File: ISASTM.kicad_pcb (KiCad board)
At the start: 4 copper layers, 101.6 x 101.6 mm, 137 parts, among them J1 Bus_ISA_8bit, J2 USB_C_Receptacle_USB2.0, J3 Boot select, J4 USB_C_Receptacle_USB2.0, J5 TagConnect_TC2030_SWD, SW1 Reset, U1 STM32H743IITx, U10 SN74AVC8T245PW, U11 SN74AVC8T245PW, U12 SN74AVC8T245PW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

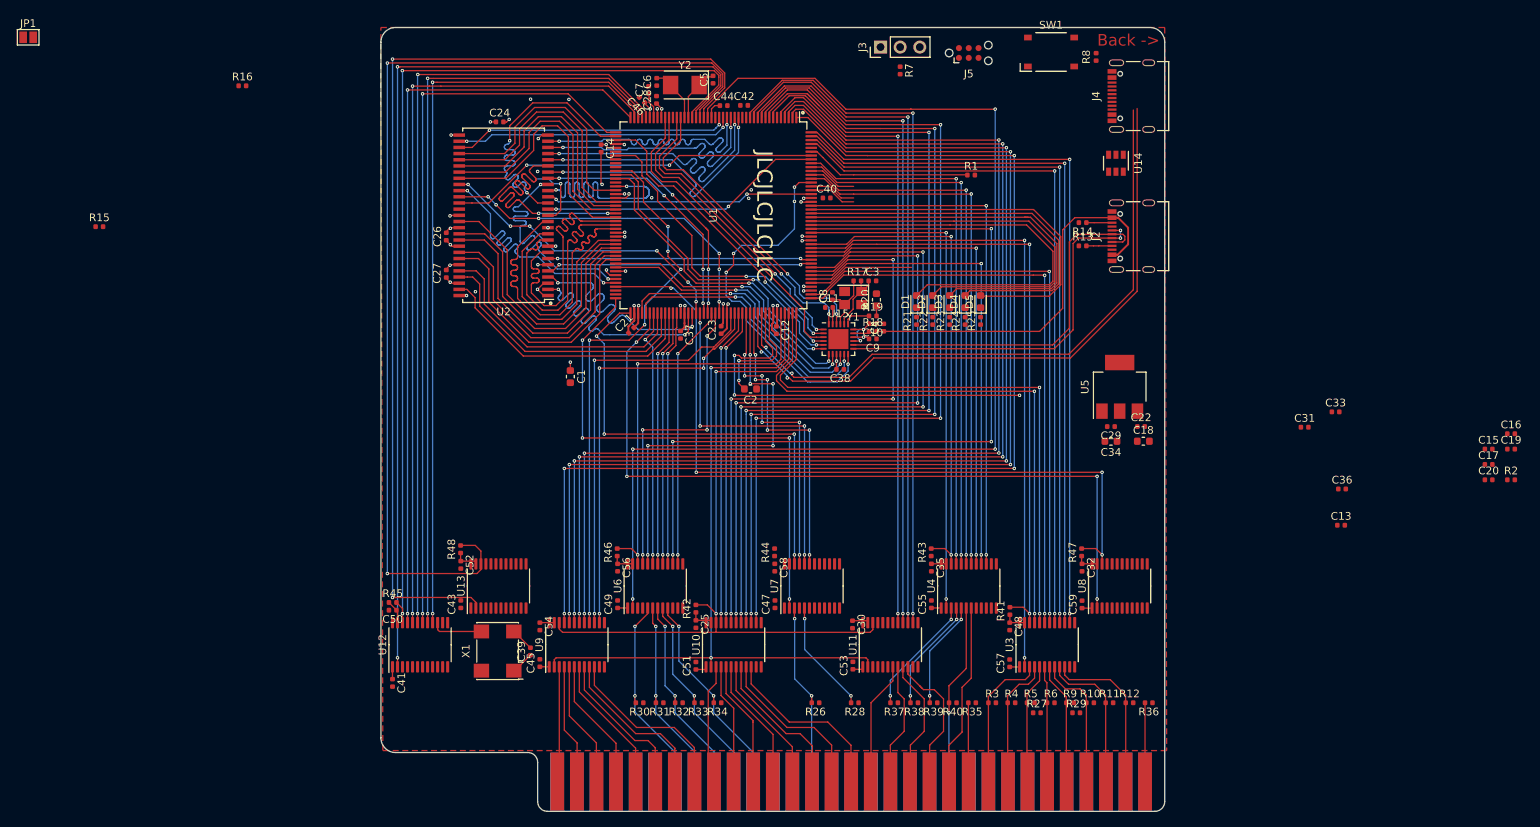
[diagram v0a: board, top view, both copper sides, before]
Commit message: Finish ISA signal routing
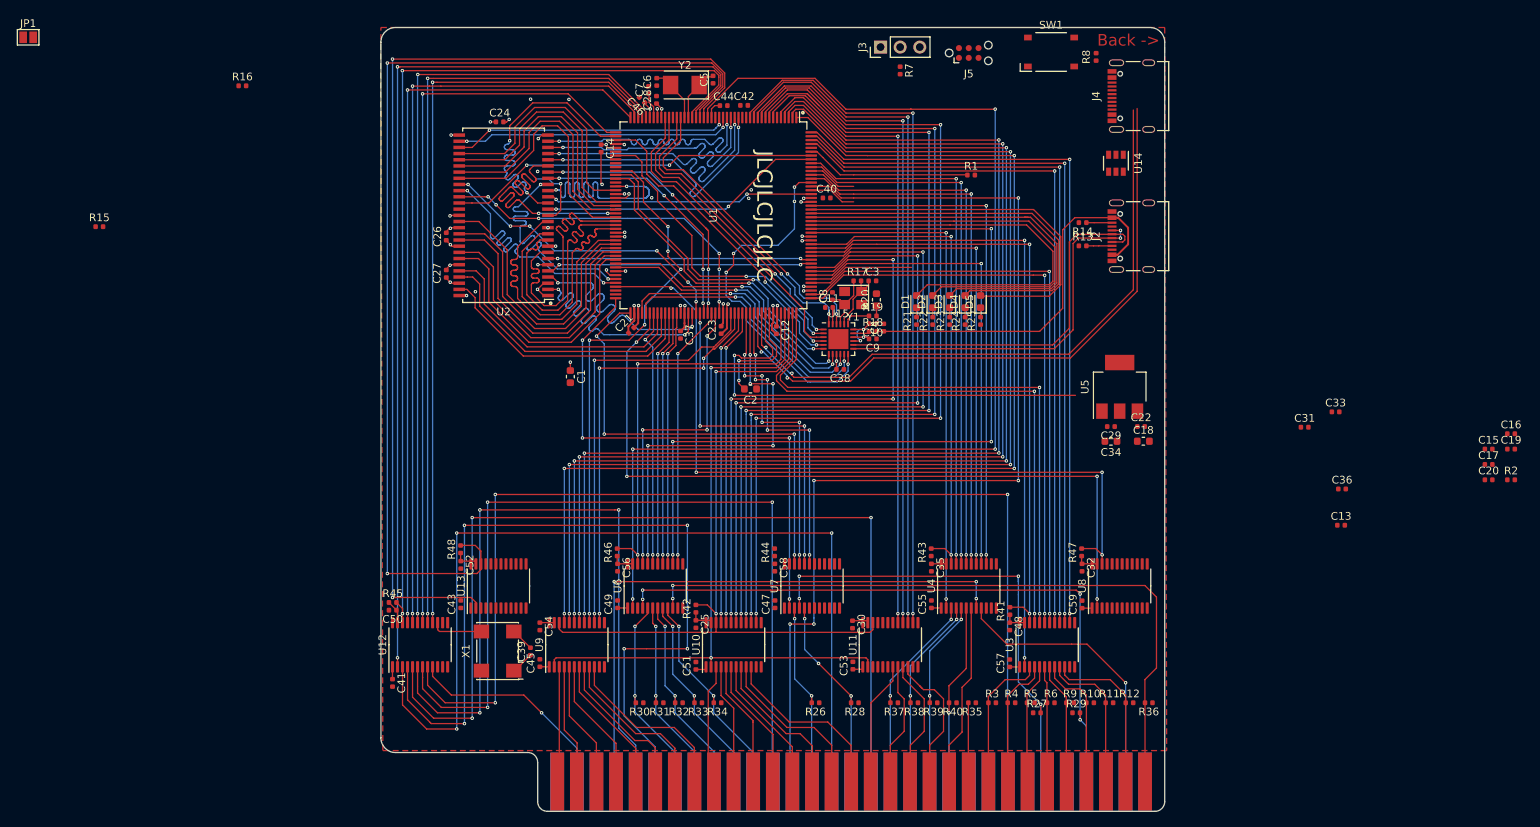
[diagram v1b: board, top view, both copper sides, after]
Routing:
- net /~NOWS: track 0.00 -> 142.8 mm, vias 0 -> 3
- net /~DACK3: track 0.00 -> 125.9 mm, vias 0 -> 3
- net /~REFRESH: track 6.12 -> 131.7 mm, vias 0 -> 5
- net /~DACK1: track 0.00 -> 119.8 mm, vias 0 -> 3
- net /CLK: track 0.00 -> 112.2 mm, vias 0 -> 3
- net /~DACK2: track 0.00 -> 110.7 mm, vias 0 -> 5
- net /TC: track 0.00 -> 93.1 mm, vias 0 -> 3
- net /IRQ2: track 0.00 -> 84.8 mm, vias 0 -> 4
- net /~IO_CH_CK: track 10.5 -> 91.1 mm, vias 0 -> 2
- net /ALE: track 0.00 -> 76.0 mm, vias 0 -> 3
- net /DRQ2: track 0.00 -> 59.7 mm, vias 0 -> 4
- net /ISARESET: track 0.00 -> 36.3 mm, vias 0 -> 1
- net /OSC: track 0.00 -> 28.2 mm, vias 0 -> 1
- net /~IOR: track 15.6 -> 27.3 mm
- net /~SMEMR: track 14.0 -> 25.4 mm
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
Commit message: Finish routing
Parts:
- C13, C17, C36: moved to B.Cu
- moved JP1 139.7 mm to (108.3, 31.8), turned to 270 degrees
- moved R15 129.1 mm to (106.9, 24.7)
- moved C17 124.5 mm to (37.9, 41.6), turned to 90 degrees
- moved R2 124.3 mm to (48.4, 22.2)
- moved R16 109.6 mm to (106.9, 21.7), turned to 180 degrees
- moved C13 109.5 mm to (34.4, 49.1), turned to 180 degrees
- moved C36 107.8 mm to (35.6, 47.0), turned to 90 degrees
- moved C31 100.0 mm to (39.1, 37.9), turned to 270 degrees
- moved C16 95.3 mm to (73.2, 31.9), turned to 315 degrees
- moved C19 92.9 mm to (73.0, 41.8)
- moved C20 90.2 mm to (71.3, 51.5), turned to 270 degrees
- moved C15 88.0 mm to (85.9, 20.0), turned to 180 degrees
- moved C33 62.7 mm to (97.2, 17.8), turned to 270 degrees
- moved C39 28.6 mm to (34.7, 66.9)
- moved X1 28.6 mm to (30.5, 66.8)
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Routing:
- net +5V: track 12.4 -> 151.8 mm, vias 1 -> 45
- net /SWDIO: track 60.5 -> 128.8 mm, vias 2 -> 6
- net /~RESET: track 40.2 -> 101.8 mm, vias 2 -> 5
- net +3V3: track 76.9 -> 135.5 mm, vias 21 -> 95
- net /IO_CH_RDY: track 10.3 -> 68.7 mm, vias 0 -> 2
- net /SWCLK: track 13.8 -> 70.3 mm, vias 0 -> 4
- net /SWO: track 6.12 -> 56.7 mm, vias 0 -> 4
- net /BOOT0: track 6.33 -> 51.5 mm, vias 0 -> 2
- net GND: track 37.1 -> 72.1 mm, vias 27 -> 116
- net Net-(J4-PadA4): track 0.00 -> 28.0 mm, vias 0 -> 6
- net Net-(U12-Pad15): track 6.65 -> 33.3 mm, vias 0 -> 2
- net /USB_FS_D+: track 82.4 -> 90.6 mm
- net /USB_FS_D-: track 84.2 -> 92.4 mm, vias 2 -> 4
- net /~CONTROL2_OE: track 60.2 -> 63.1 mm
- net Net-(J4-PadA5): track 0.00 -> 2.74 mm
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- added copper zone on F.Cu, net +3V3
- added copper zone on In2.Cu, net +5V
- added copper zone on B.Cu, net GND

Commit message: Stitch board edge
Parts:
- moved C43 0.14 mm to (25.6, 89.5)
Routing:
- net GND: vias 116 -> 389

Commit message: Finish GND stitching
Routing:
- net GND: vias 389 -> 470
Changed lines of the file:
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@@
     (thickness 1.6)
     (drawings 35)
-    (tracks 4887)
+    (tracks 4968)
     (zones 0)
     (modules 137)
@@
   (gr_arc (start 115.57 114.935) (end 115.57 116.205) (angle -90) (layer Edge.Cuts) (width 0.05))
   (gr_arc (start 36.83 114.935) (end 35.56 114.935) (angle -90) (layer Edge.Cuts) (width 0.05))
+  (via (at 55.9 79.6) (size 0.45) (drill 0.2) (layers F.Cu B.Cu) (net 32))
+  (via (at 55.9 80.6) (size 0.45) (drill 0.2) (layers F.Cu B.Cu) (net 32))
+  (via (at 55.9 75.6) (size 0.45) (drill 0.2) (layers F.Cu B.Cu) (net 32))
+  (via (at 55.9 78.6) (size 0.45) (drill 0.2) (layers F.Cu B.Cu) (net 32))
+  (via (at 55.9 74.6) (size 0.45) (drill 0.2) (layers F.Cu B.Cu) (net 32))
+  (via (at 55.9 77.6) (size 0.45) (drill 0.2) (layers F.Cu B.Cu) (net 32))
+  (via (at 55.9 76.6) (size 0.45) (drill 0.2) (layers F.Cu B.Cu) (net 32))
+  (via (at 47.4 79.6) (size 0.45) (drill 0.2) (layers F.Cu B.Cu) (net 32))
+  (via (at 47.4 80.6) (size 0.45) (drill 0.2) (layers F.Cu B.Cu) (net 32))
+  (via (at 47.4 75.6) (size 0.45) (drill 0.2) (layers F.Cu B.Cu) (net 32))
+  (via (at 47.4 78.6) (size 0.45) (drill 0.2) (layers F.Cu B.Cu) (net 32))
+  (via (at 47.4 74.6) (size 0.45) (drill 0.2) (layers F.Cu B.Cu) (net 32))
+  (via (at 47.4 77.6) (size 0.45) (drill 0.2) (layers F.Cu B.Cu) (net 32))
+  (via (at 47.4 76.6) (size 0.45) (drill 0.2) (layers F.Cu B.Cu) (net 32))
   (via (at 46.8 53.65) (size 0.45) (drill 0.2) (layers F.Cu B.Cu) (net 32))
   (via (at 73.6 56) (size 0.45) (drill 0.2) (layers F.Cu B.Cu) (net 32))
@@
   (via (at 116.4 107) (size 0.45) (drill 0.2) (layers F.Cu B.Cu) (net 32))
   (via (at 116.4 108) (size 0.45) (drill 0.2) (layers F.Cu B.Cu) (net 32))
+  (via (at 69.8 32.2) (size 0.45) (drill 0.2) (layers F.Cu B.Cu) (net 32))
+  (via (at 69.8 34.2) (size 0.45) (drill 0.2) (layers F.Cu B.Cu) (net 32))
+  (via (at 69.7 35.5) (size 0.45) (drill 0.2) (layers F.Cu B.Cu) (net 32))
+  (via (at 62.6 45.9) (size 0.45) (drill 0.2) (layers F.Cu B.Cu) (net 32))
+  (via (at 58.4 46.4) (size 0.45) (drill 0.2) (layers F.Cu B.Cu) (net 32))
+  (via (at 58.4 54.7) (size 0.45) (drill 0.2) (layers F.Cu B.Cu) (net 32))
+  (via (at 54.9 56.9) (size 0.45) (drill 0.2) (layers F.Cu B.Cu) (net 32))
+  (via (at 55.6 54.2) (size 0.45) (drill 0.2) (layers F.Cu B.Cu) (net 32))
+  (via (at 54.05 53.05) (size 0.45) (drill 0.2) (layers F.Cu B.Cu) (net 32))
+  (via (at 50.4 50.4) (size 0.45) (drill 0.2) (layers F.Cu B.Cu) (net 32))
+  (via (at 49.4 48.8) (size 0.45) (drill 0.2) (layers F.Cu B.Cu) (net 32))
+  (via (at 46.5 50.8) (size 0.45) (drill 0.2) (layers F.Cu B.Cu) (net 32))
+  (via (at 43.8 53.3) (size 0.45) (drill 0.2) (layers F.Cu B.Cu) (net 32))
+  (via (at 42.6 54.6) (size 0.45) (drill 0.2) (layers F.Cu B.Cu) (net 32))
+  (via (at 45.2 53.6) (size 0.45) (drill 0.2) (layers F.Cu B.Cu) (net 32))
+  (via (at 40.6 57.7) (size 0.45) (drill 0.2) (layers F.Cu B.Cu) (net 32))
+  (via (at 22.4 63.6) (size 0.45) (drill 0.2) (layers F.Cu B.Cu) (net 32))
+  (via (at 23.1 88) (size 0.45) (drill 0.2) (layers F.Cu B.Cu) (net 32))
+  (via (at 24.6 88) (size 0.45) (drill 0.2) (layers F.Cu B.Cu) (net 32))
+  (via (at 24.6 84.9) (size 0.45) (drill 0.2) (layers F.Cu B.Cu) (net 32))
+  (via (at 23.1 84.9) (size 0.45) (drill 0.2) (layers F.Cu B.Cu) (net 32))
+  (via (at 25.4 79.5) (size 0.45) (drill 0.2) (layers F.Cu B.Cu) (net 32))
+  (via (at 26.5 78.5) (size 0.45) (drill 0.2) (layers F.Cu B.Cu) (net 32))
+  (via (at 27.5 77.6) (size 0.45) (drill 0.2) (layers F.Cu B.Cu) (net 32))
+  (via (at 28.5 76.6) (size 0.45) (drill 0.2) (layers F.Cu B.Cu) (net 32))
+  (via (at 29.5 75.6) (size 0.45) (drill 0.2) (layers F.Cu B.Cu) (net 32))
+  (via (at 38.5 74.6) (size 0.45) (drill 0.2) (layers F.Cu B.Cu) (net 32))
+  (via (at 38.5 80.6) (size 0.45) (drill 0.2) (layers F.Cu B.Cu) (net 32))
+  (via (at 38.5 79.6) (size 0.45) (drill 0.2) (layers F.Cu B.Cu) (net 32))
+  (via (at 38.5 78.6) (size 0.45) (drill 0.2) (layers F.Cu B.Cu) (net 32))
+  (via (at 38.5 77.6) (size 0.45) (drill 0.2) (layers F.Cu B.Cu) (net 32))
+  (via (at 38.5 76.6) (size 0.45) (drill 0.2) (layers F.Cu B.Cu) (net 32))
+  (via (at 38.5 75.6) (size 0.45) (drill 0.2) (layers F.Cu B.Cu) (net 32))
+  (via (at 66.9 68.8) (size 0.45) (drill 0.2) (layers F.Cu B.Cu) (net 32))
+  (via (at 71.4 67.5) (size 0.45) (drill 0.2) (layers F.Cu B.Cu) (net 32))
+  (via (at 71.4 68.8) (size 0.45) (drill 0.2) (layers F.Cu B.Cu) (net 32))
+  (via (at 94.2 74.2) (size 0.45) (drill 0.2) (layers F.Cu B.Cu) (net 32))
+  (via (at 84.8 74.3) (size 0.45) (drill 0.2) (layers F.Cu B.Cu) (net 32))
+  (via (at 71.9 76.6) (size 0.45) (drill 0.2) (layers F.Cu B.Cu) (net 32))
+  (via (at 67.1 81.1) (size 0.45) (drill 0.2) (layers F.Cu B.Cu) (net 32))
+  (via (at 70.7 88.7) (size 0.45) (drill 0.2) (layers F.Cu B.Cu) (net 32))
+  (via (at 88.3 28.7) (size 0.45) (drill 0.2) (layers F.Cu B.Cu) (net 32))
+  (via (at 85.2 28.7) (size 0.45) (drill 0.2) (layers F.Cu B.Cu) (net 32))
+  (via (at 93.2 28.7) (size 0.45) (drill 0.2) (layers F.Cu B.Cu) (net 32))
+  (via (at 96.9 29.7) (size 0.45) (drill 0.2) (layers F.Cu B.Cu) (net 32))
+  (via (at 91.8 34.5) (size 0.45) (drill 0.2) (layers F.Cu B.Cu) (net 32))
+  (via (at 92.7 35.9) (size 0.45) (drill 0.2) (layers F.Cu B.Cu) (net 32))
+  (via (at 94.4 37.7) (size 0.45) (drill 0.2) (layers F.Cu B.Cu) (net 32))
+  (via (at 97.9 35.9) (size 0.45) (drill 0.2) (layers F.Cu B.Cu) (net 32))
+  (via (at 99.2 36.7) (size 0.45) (drill 0.2) (layers F.Cu B.Cu) (net 32))
+  (via (at 106.1 85.8) (size 0.45) (drill 0.2) (layers F.Cu B.Cu) (net 32))
+  (via (at 106.7 88.5) (size 0.45) (drill 0.2) (layers F.Cu B.Cu) (net 32))
+  (via (at 100.3 60.6) (size 0.45) (drill 0.2) (layers F.Cu B.Cu) (net 32))
+  (via (at 101.2 44.2) (size 0.45) (drill 0.2) (layers F.Cu B.Cu) (net 32))
+  (via (at 93.1 44) (size 0.45) (drill 0.2) (layers F.Cu B.Cu) (net 32))
+  (via (at 98.9 41.3) (size 0.45) (drill 0.2) (layers F.Cu B.Cu) (net 32))
+  (via (at 32.6 65.7) (size 0.45) (drill 0.2) (layers F.Cu B.Cu) (net 32))
+  (via (at 41.1 94.7) (size 0.45) (drill 0.2) (layers F.Cu B.Cu) (net 32))
+  (via (at 25.6 91.9) (size 0.45) (drill 0.2) (layers F.Cu B.Cu) (net 32))
+  (via (at 26.6 91.9) (size 0.45) (drill 0.2) (layers F.Cu B.Cu) (net 32))
+  (via (at 25.6 88) (size 0.45) (drill 0.2) (layers F.Cu B.Cu) (net 32))
+  (via (at 26.6 88) (size 0.45) (drill 0.2) (layers F.Cu B.Cu) (net 32))
+  (via (at 24.6 89.2) (size 0.45) (drill 0.2) (layers F.Cu B.Cu) (net 32))
+  (via (at 44.2 90.6) (size 0.45) (drill 0.2) (layers F.Cu B.Cu) (net 32))
+  (via (at 47.7 58.2) (size 0.45) (drill 0.2) (layers F.Cu B.Cu) (net 32))
+  (via (at 45.7 58.2) (size 0.45) (drill 0.2) (layers F.Cu B.Cu) (net 32))
+  (via (at 39.9 70.3) (size 0.45) (drill 0.2) (layers F.Cu B.Cu) (net 32))
   (via (at 111.1 68.3) (size 0.45) (drill 0.2) (layers F.Cu B.Cu) (net 61))
   (via (at 111.3 70.2) (size 0.45) (drill 0.2) (layers F.Cu B.Cu) (net 61))

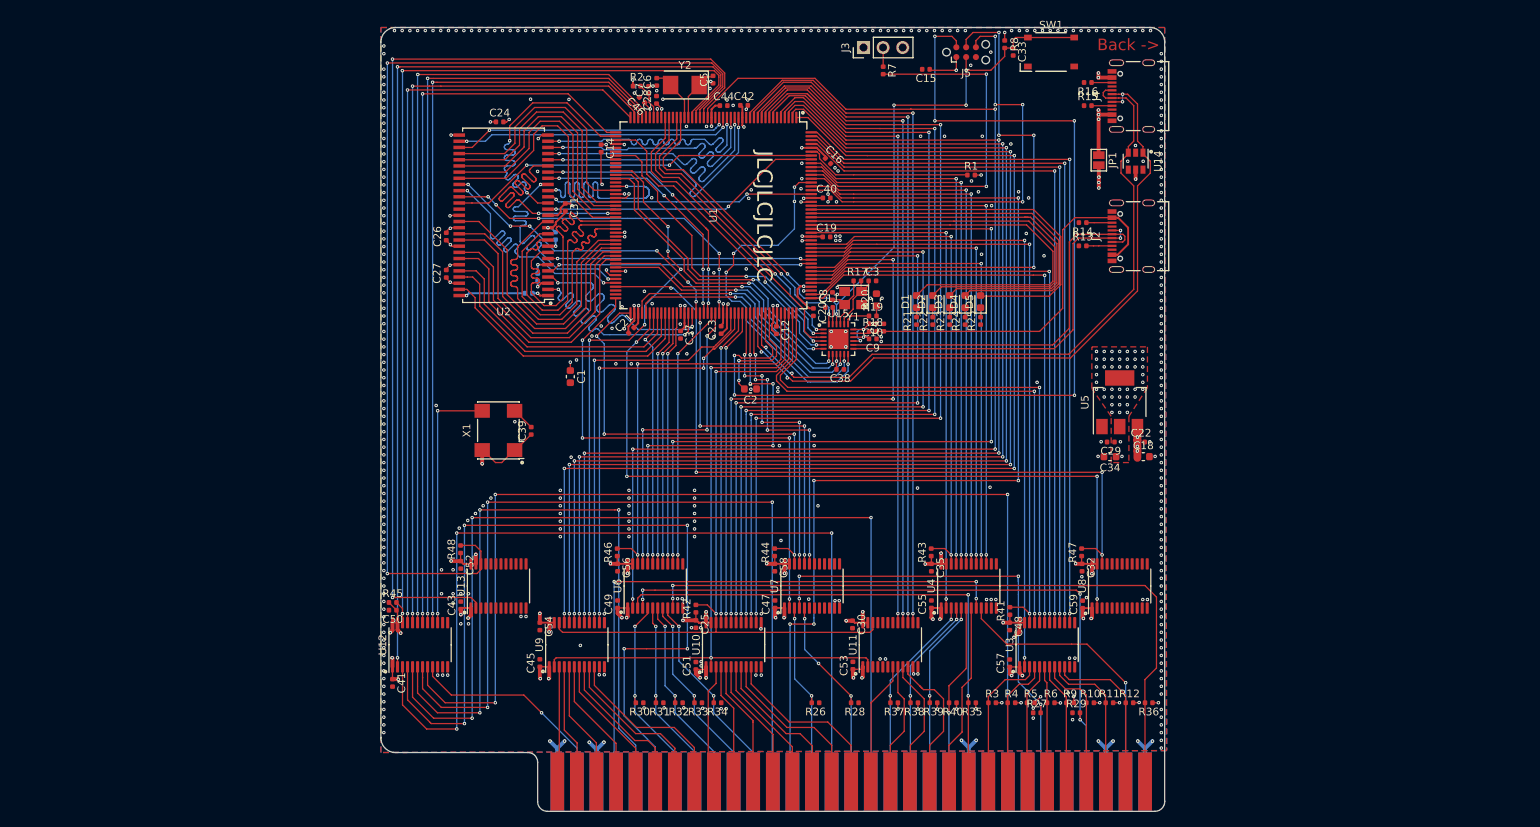
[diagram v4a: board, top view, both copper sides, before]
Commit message: Hide all footprint references
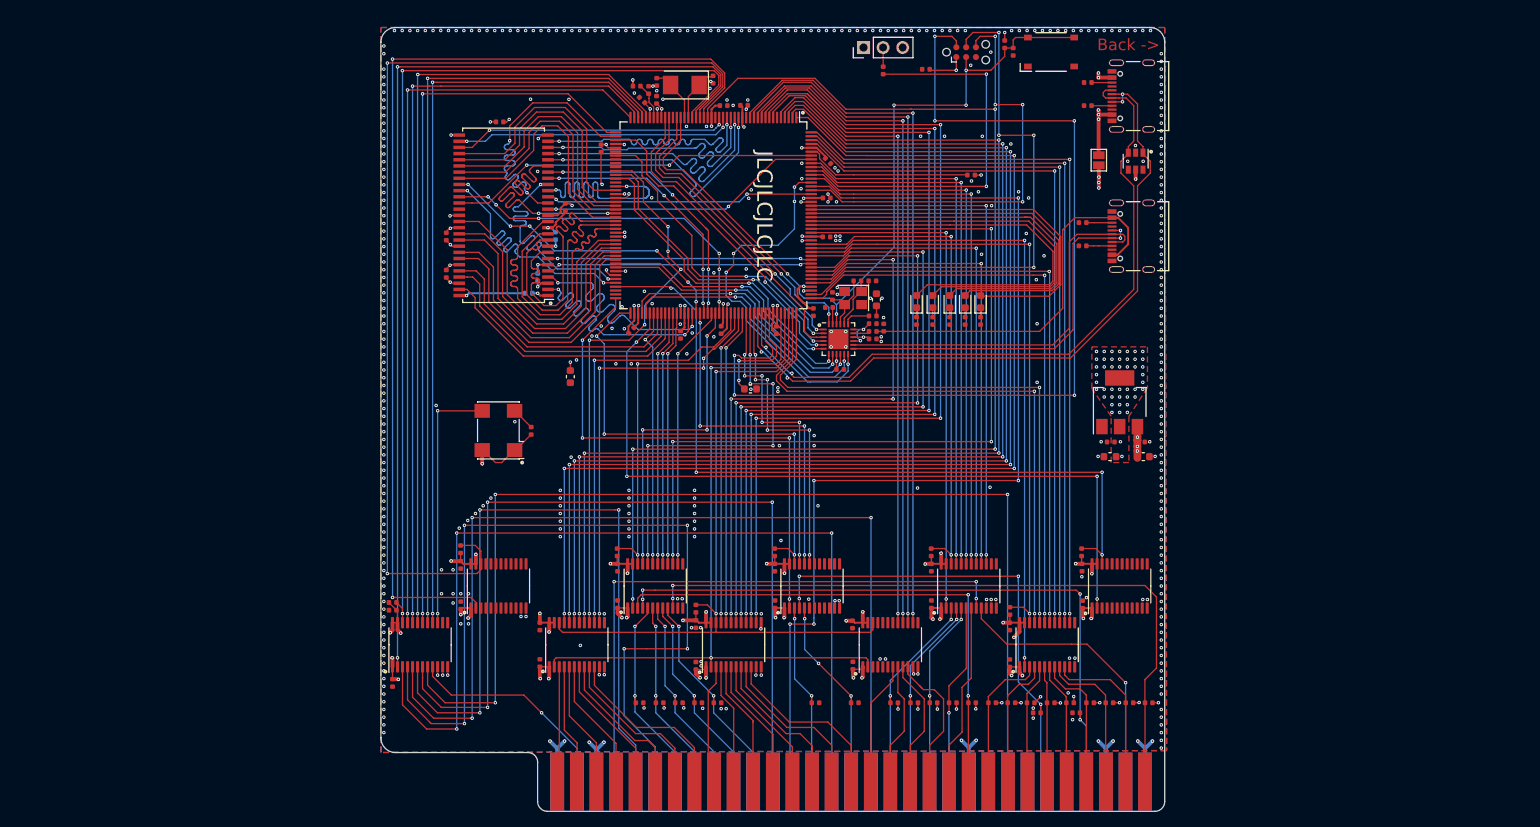
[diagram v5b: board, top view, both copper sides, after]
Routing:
- net GND: vias 470 -> 473
